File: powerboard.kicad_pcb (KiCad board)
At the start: 2 copper layers, 81.3 x 61.6 mm, 24 parts, among them J1 B03B, J2 EMER_SW, J3 EMER_SW, Q1 TJ60S04M3L, U1 TLP222A

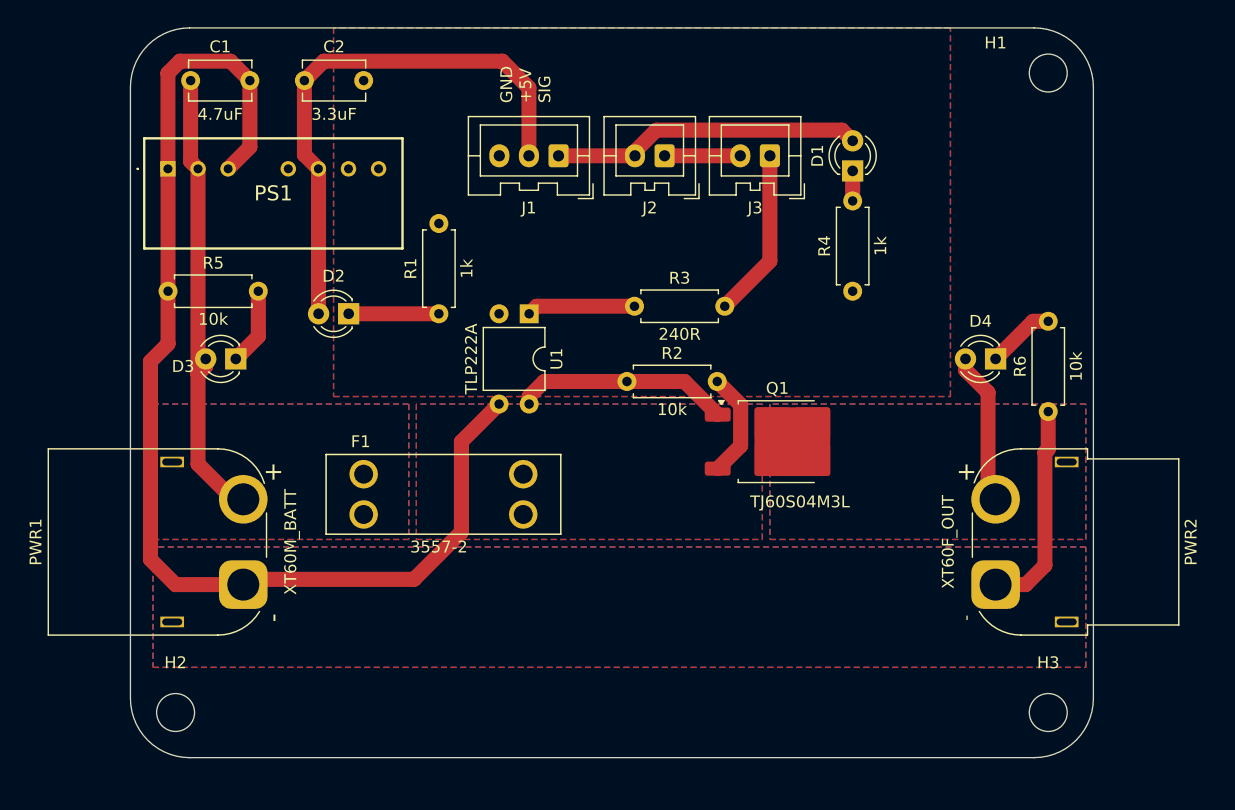
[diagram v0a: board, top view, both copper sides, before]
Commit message: pcb/sch: add a hole, silks
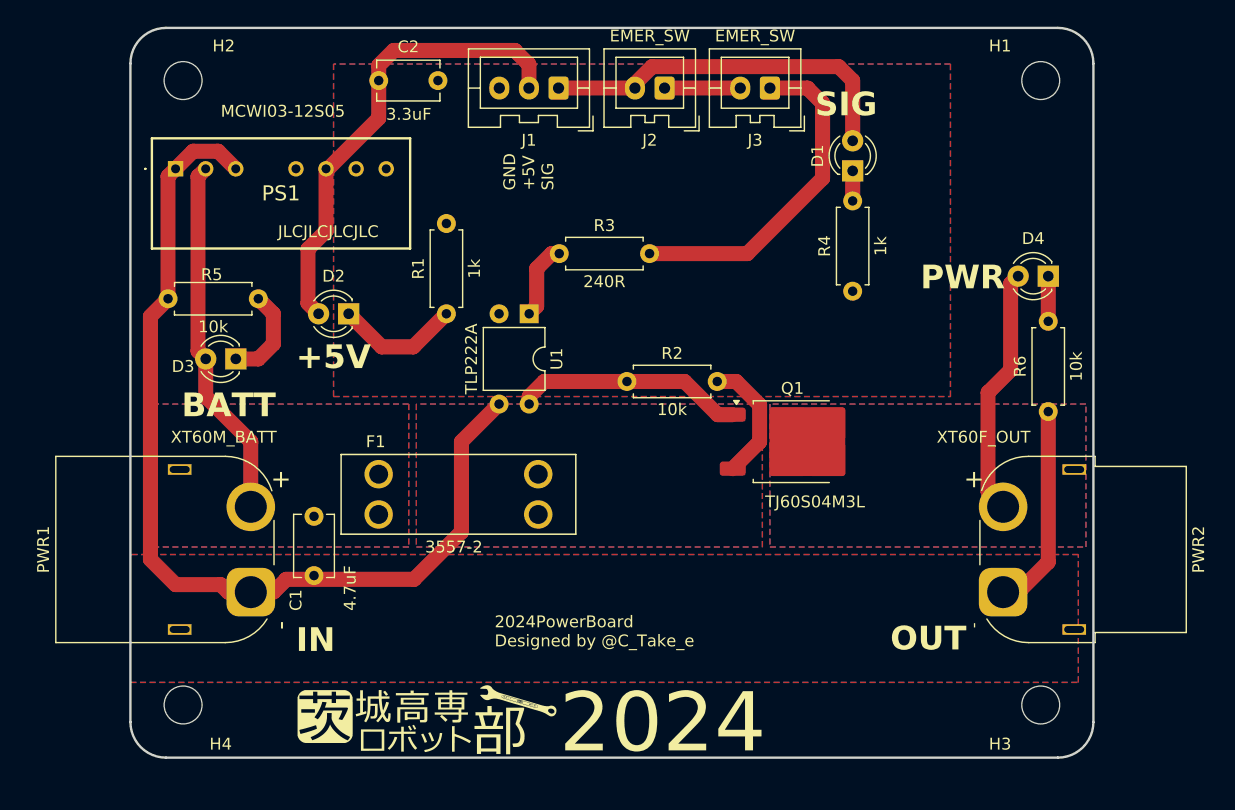
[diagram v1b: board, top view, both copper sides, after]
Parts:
- added G***: LOGO, LOGO, F.Cu at (141.0, 142.2)
- added H4: MountingHole, MountingHole:MountingHole_3.2mm_M3, F.Cu at (120.0, 141.0)
- moved H2 53.3 mm to (120.0, 88.3)
- moved C1 38.2 mm to (131.1, 125.0), turned to -90 degrees
- moved D4 8.28 mm to (193.0, 104.8)
- moved R3 7.75 mm to (159.4, 102.9)
- moved C2 6.27 mm to (136.5, 88.3)
- moved J1 5.71 mm to (151.7, 88.9)
- moved J2 5.71 mm to (160.7, 88.9)
- moved J3 5.71 mm to (169.5, 88.9)
- moved Q1 1.27 mm to (171.4, 118.7)
- moved F1 1.27 mm to (143.3, 123.2)
- moved H1 0.90 mm to (192.4, 88.3)
- moved PWR1 0.90 mm to (125.7, 131.4)
- moved H3 0.90 mm to (192.4, 141.0)
- moved PWR2 0.90 mm to (189.2, 131.4)
- moved PS1 0.64 mm to (119.4, 95.7)
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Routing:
- net GNDPWR: track 116.9 -> 99.3 mm
- net Net-(J3-Pin_1): track 14.3 -> 28.6 mm
- net VOUT: track 12.9 -> 21.0 mm
- net BATT: track 39.2 -> 31.4 mm
- net +5V: track 46.5 -> 39.6 mm
- net sig: track 26.3 -> 31.4 mm
- net Net-(D2-K): track 7.61 -> 10.6 mm
- net Net-(R3-Pad2): track 9.15 -> 6.50 mm
- net Net-(D4-K): track 5.76 -> 3.81 mm
- net VDD: track 8.98 -> 10.7 mm
- net Net-(D3-K): track 6.50 -> 8.03 mm
- net FET_G: track 18.2 -> 19.5 mm
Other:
- outline, holes or cut-outs redrawn
- board text added: "+5V"
- board text added: "2024"
- board text added: "2024PowerBoard Designed by @C_Take_e"
- board text added: "BATT"
- board text added: "IN"
- board text added: "JLCJLCJLCJLC"
- board text added: "MCWI03-12S05"
- board text added: "OUT"
- board text added: "PWR"
- board text added: "SIG"

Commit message: pcb: update with sch, add CUTE RESISTOR
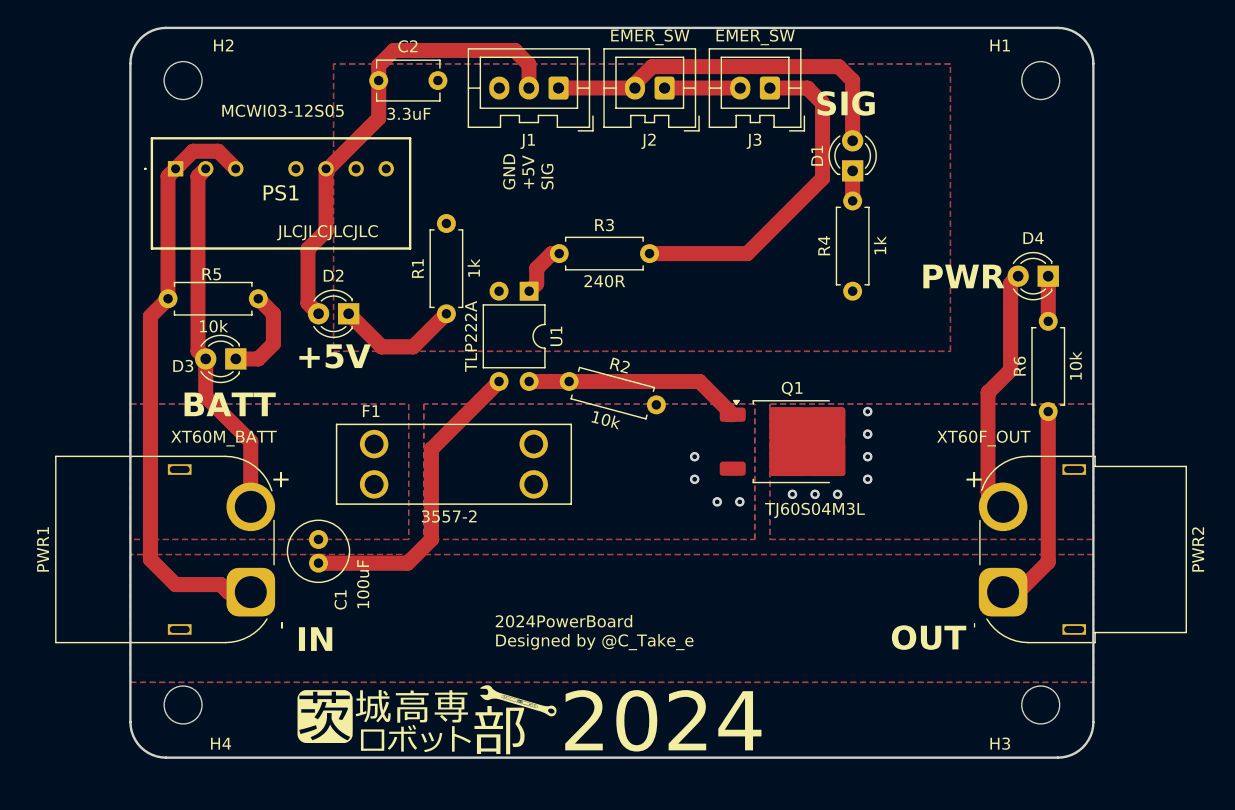
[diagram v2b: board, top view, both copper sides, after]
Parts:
- C1: value 4.7uF -> 100uF; footprint Capacitor_THT:C_Disc_D5.1mm_W3.2mm_P5.00mm -> Capacitor_THT:C_Radial_D5.0mm_H11.0mm_P2.00mm
- moved R2 5.50 mm to (160.0, 115.6), turned to 165 degrees
- moved F1 2.57 mm to (142.9, 120.7)
- moved C1 1.99 mm to (131.4, 127.0)
- moved U1 1.91 mm to (149.2, 106.0)
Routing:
- net VDD: track 10.7 -> 0.00 mm, vias 0 -> 4
- net GNDPWR: track 99.3 -> 93.4 mm
- net Net-(R3-Pad2): track 6.50 -> 4.60 mm
- net FET_G: track 19.5 -> 18.6 mm
- net VOUT: vias 0 -> 7

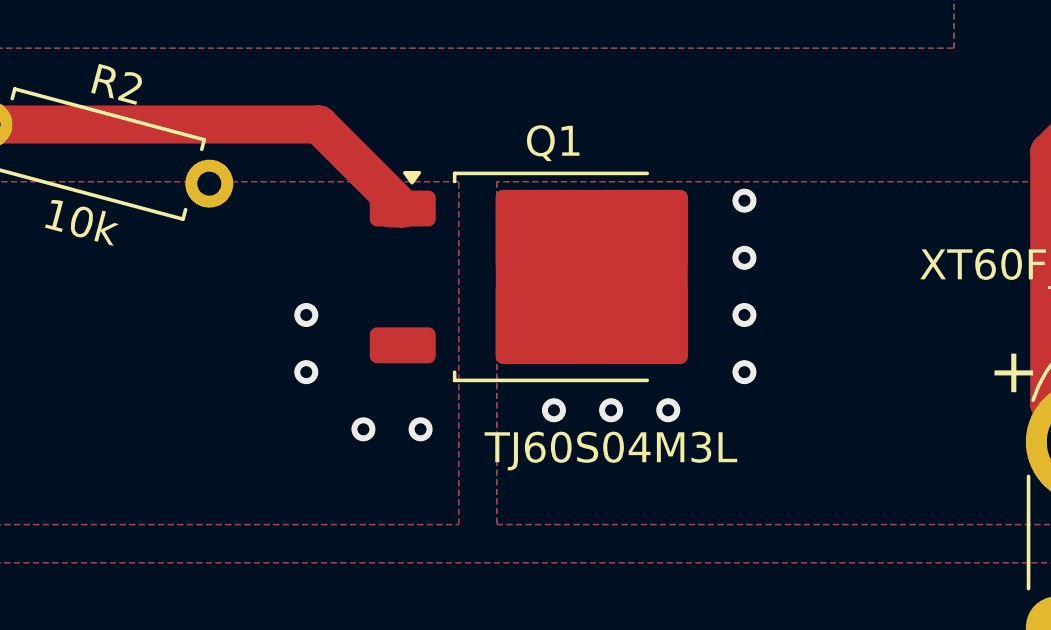
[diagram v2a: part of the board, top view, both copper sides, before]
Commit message: pcb: add vias
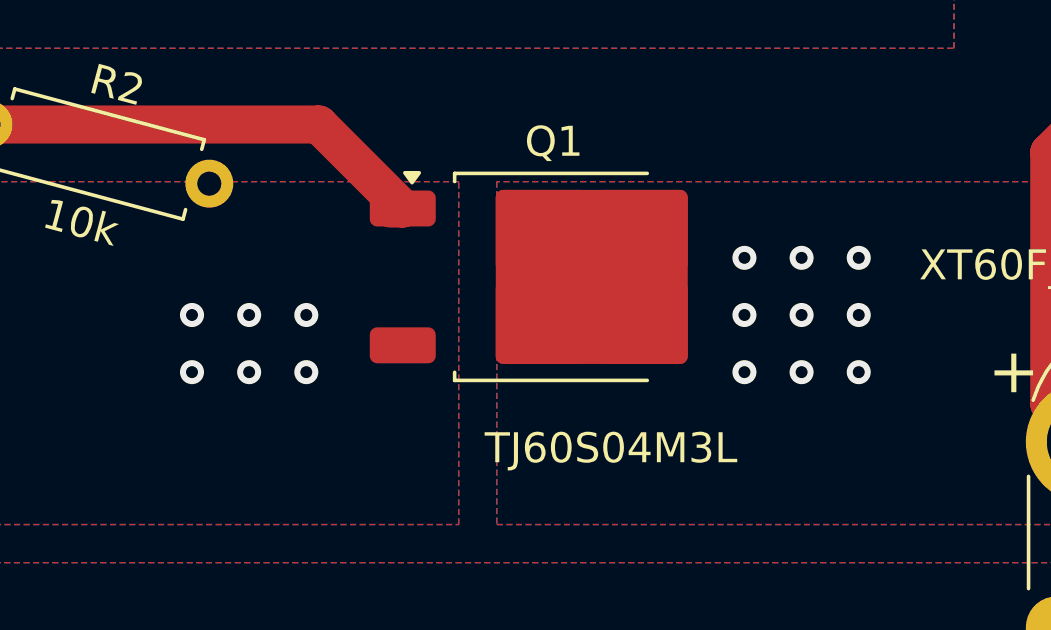
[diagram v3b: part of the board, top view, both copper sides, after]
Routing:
- net VOUT: vias 7 -> 9
- net VDD: vias 4 -> 6
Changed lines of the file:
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@@
+	)
+	(via
+		(at 159.385 121.92)
+		(size 0.8)
+		(drill 0.4)
+		(layers "F.Cu" "B.Cu")
+		(free yes)
+		(net 6)
+	)
+	(via
+		(at 161.29 120.015)
+		(size 0.8)
+		(drill 0.4)
+		(layers "F.Cu" "B.Cu")
+		(free yes)
+		(net 6)
 	)
 	(via
@@
 	)
 	(via
-		(at 167.005 123.825)
+		(at 161.29 121.92)
 		(size 0.8)
 		(drill 0.4)
@@
 	)
 	(via
-		(at 165.1 123.825)
+		(at 159.385 120.015)
 		(size 0.8)
 		(drill 0.4)
@@
 	)
 	(via
-		(at 173.355 123.19)
-		(size 0.8)
-		(drill 0.4)
-		(layers "F.Cu" "B.Cu")
-		(free yes)
-		(net 15)
-	)
-	(via
-		(at 175.26 123.19)
+		(at 179.705 118.11)
+		(size 0.8)
+		(drill 0.4)
+		(layers "F.Cu" "B.Cu")
+		(free yes)
+		(net 15)
+	)
+	(via
+		(at 181.61 121.92)
 		(size 0.8)
 		(drill 0.4)
@@
 	)
 	(via
-		(at 177.8 116.205)
+		(at 181.61 118.11)
+		(size 0.8)
+		(drill 0.4)
+		(layers "F.Cu" "B.Cu")
+		(free yes)
+		(net 15)
+	)
+	(via
+		(at 179.705 120.015)
 		(size 0.8)
 		(drill 0.4)
@@
 	)
 	(via
-		(at 171.45 123.19)
-		(size 0.8)
-		(drill 0.4)
+		(at 179.705 121.92)
+		(size 0.8)
+		(drill 0.4)
+		(layers "F.Cu" "B.Cu")
+		(free yes)
+		(net 15)
+	)
+	(via
+		(at 181.61 120.015)
+		(size 0.8)
+		(drill 0.4)

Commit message: pcb/pdf: printed gerb
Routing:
- net Net-(D2-K): track 10.6 -> 9.83 mm
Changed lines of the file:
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@@
 	)
 	(segment
-		(start 139.446 110.744)
-		(end 142.24 107.95)
+		(start 135.895 109.855)
+		(end 140.335 109.855)
 		(width 1.27)
 		(layer "F.Cu")
@@
 	(segment
 		(start 133.99 107.95)
-		(end 136.784 110.744)
+		(end 135.895 109.855)
 		(width 1.27)
 		(layer "F.Cu")
@@
 	)
 	(segment
-		(start 136.784 110.744)
-		(end 139.446 110.744)
+		(start 140.335 109.855)
+		(end 142.24 107.95)
 		(width 1.27)
 		(layer "F.Cu")

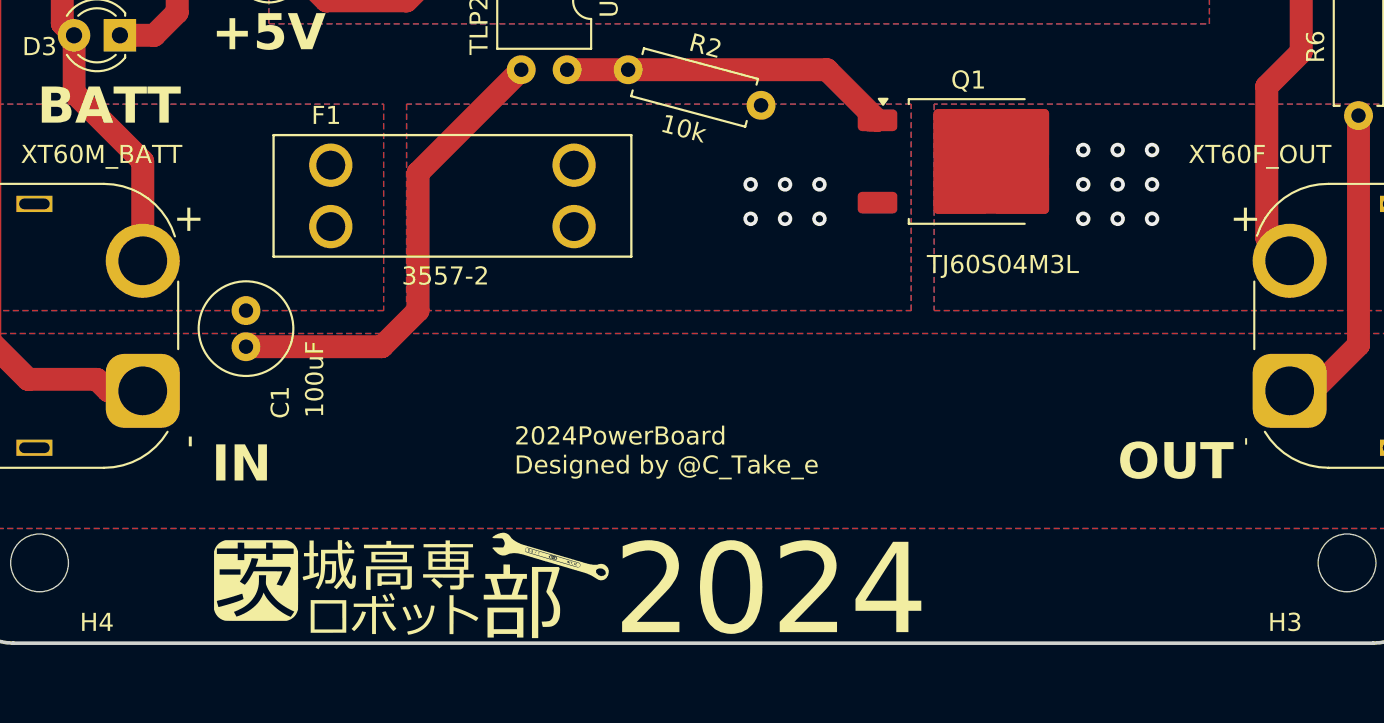
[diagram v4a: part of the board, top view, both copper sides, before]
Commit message: pcb: add vias
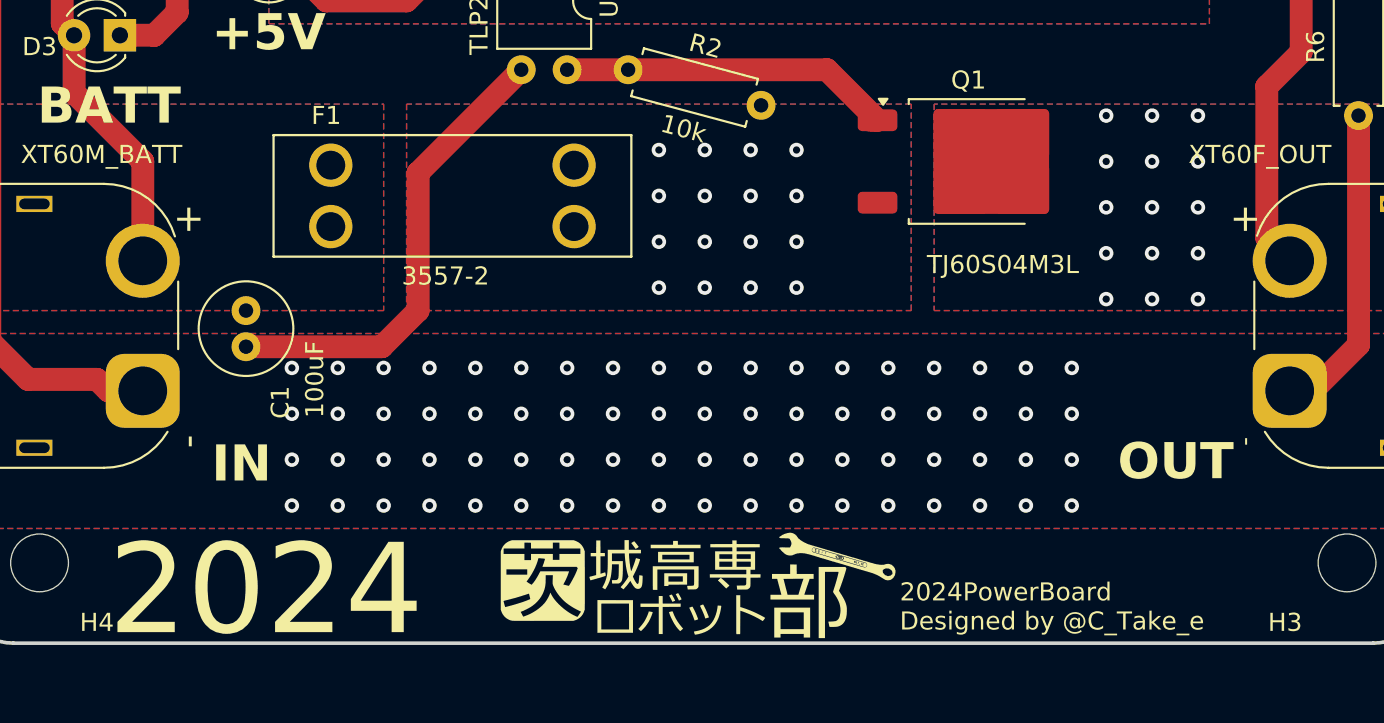
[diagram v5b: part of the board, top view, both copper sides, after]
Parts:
- moved G*** 15.9 mm to (156.8, 142.2)
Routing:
- net VOUT: vias 9 -> 15
- net VDD: vias 6 -> 16
- net GNDPWR: vias 0 -> 72
